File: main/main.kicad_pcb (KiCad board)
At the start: 2 copper layers, 25 x 29 mm, 13 parts, among them J1 PROG, SW1 CONFIG, U1 MSP430FR2311IPW16R, U2 RFM64W

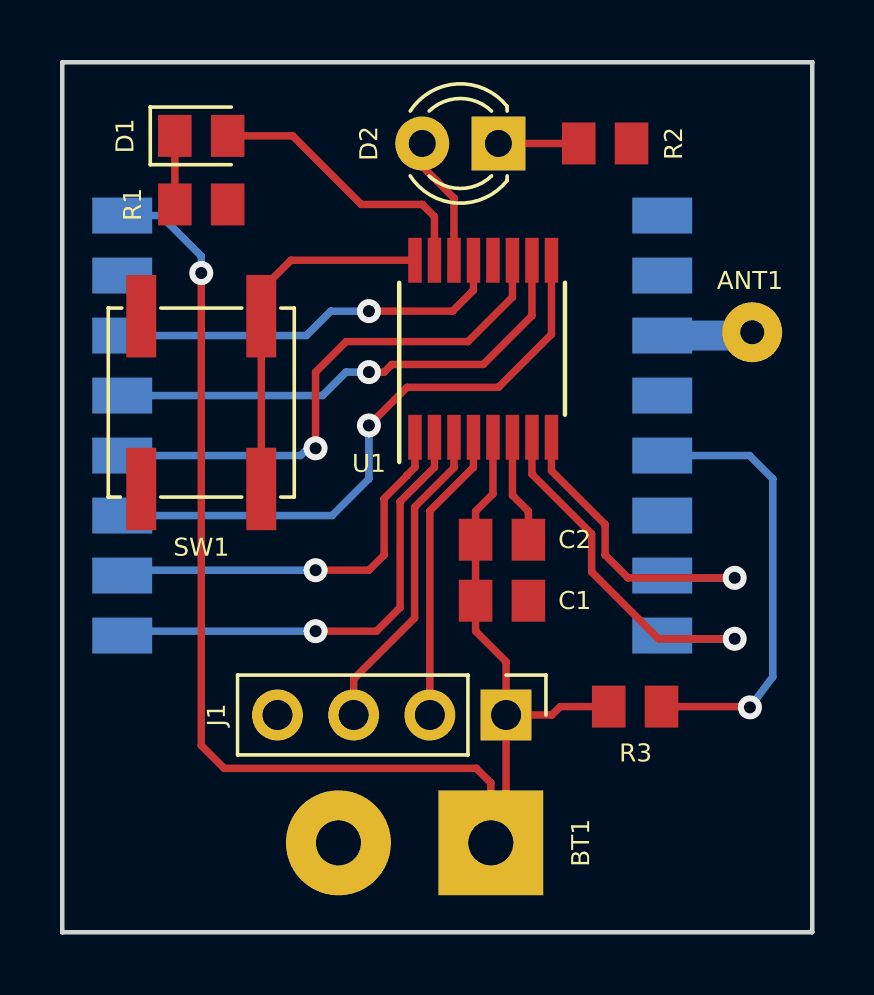
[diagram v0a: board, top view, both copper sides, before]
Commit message: Reduced board size
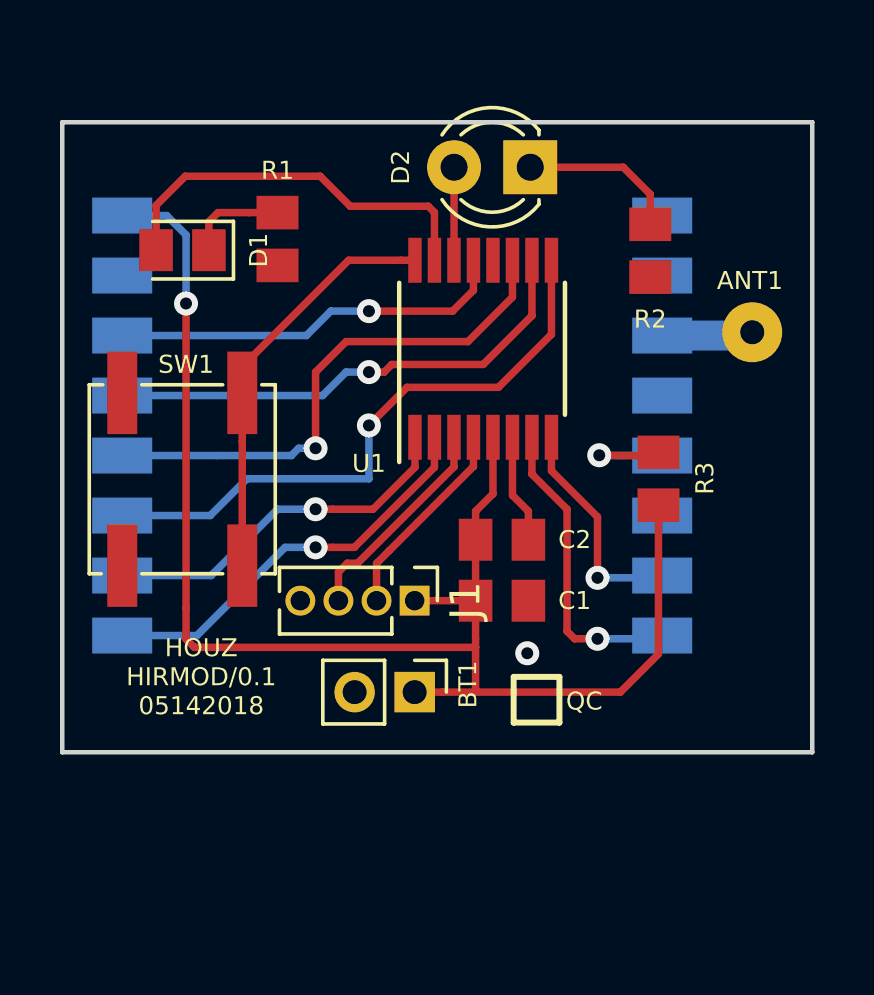
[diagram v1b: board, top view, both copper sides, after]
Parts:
- BT1: footprint Connector_Wire:SolderWirePad_1x02_P5.08mm_Drill1.5mm -> Connector_PinHeader_2.00mm:PinHeader_1x02_P2.00mm_Vertical
- J1: footprint Connector_PinHeader_2.54mm:PinHeader_1x04_P2.54mm_Vertical -> Connector_PinHeader_1.27mm:PinHeader_1x04_P1.27mm_Vertical
- moved R3 7.63 mm to (134.9, 87.9), turned to 90 degrees
- moved BT1 5.63 mm to (126.7, 95.0), turned to 270 degrees
- moved J1 4.88 mm to (126.7, 91.9)
- moved R2 3.88 mm to (134.6, 80.3), turned to 270 degrees
- moved D1 3.86 mm to (119.0, 80.3), turned to 180 degrees
- moved R1 2.79 mm to (122.2, 79.9), turned to 270 degrees
- moved SW1 2.63 mm to (119.0, 87.9)
- moved D2 1.32 mm to (130.6, 77.5)
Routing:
- net /RF_DATA: track 14.8 -> 4.22 mm
- net /IRQ_1: track 11.7 -> 7.66 mm
- net /STATUS: track 9.46 -> 13.3 mm
- net /TST: track 10.6 -> 7.24 mm
- net /RST: track 9.86 -> 6.79 mm
- net /IRQ_0: track 13.5 -> 10.5 mm
- net Net-(D2-Pad1): track 2.68 -> 5.37 mm
- net /POR: track 15.8 -> 13.7 mm
- net /PB_CFG: track 12.2 -> 13.9 mm
- net /IR: track 4.33 -> 3.10 mm
- net /NSS_CFG: track 13.4 -> 12.3 mm
- net Net-(D1-Pad1): track 2.29 -> 3.36 mm
- net GND: vias 0 -> 1
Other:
- board size 25 x 29 mm -> 25 x 21 mm
- board text added: "HOUZ HIRMOD/0.1 05142018"
- board text added: "QC"

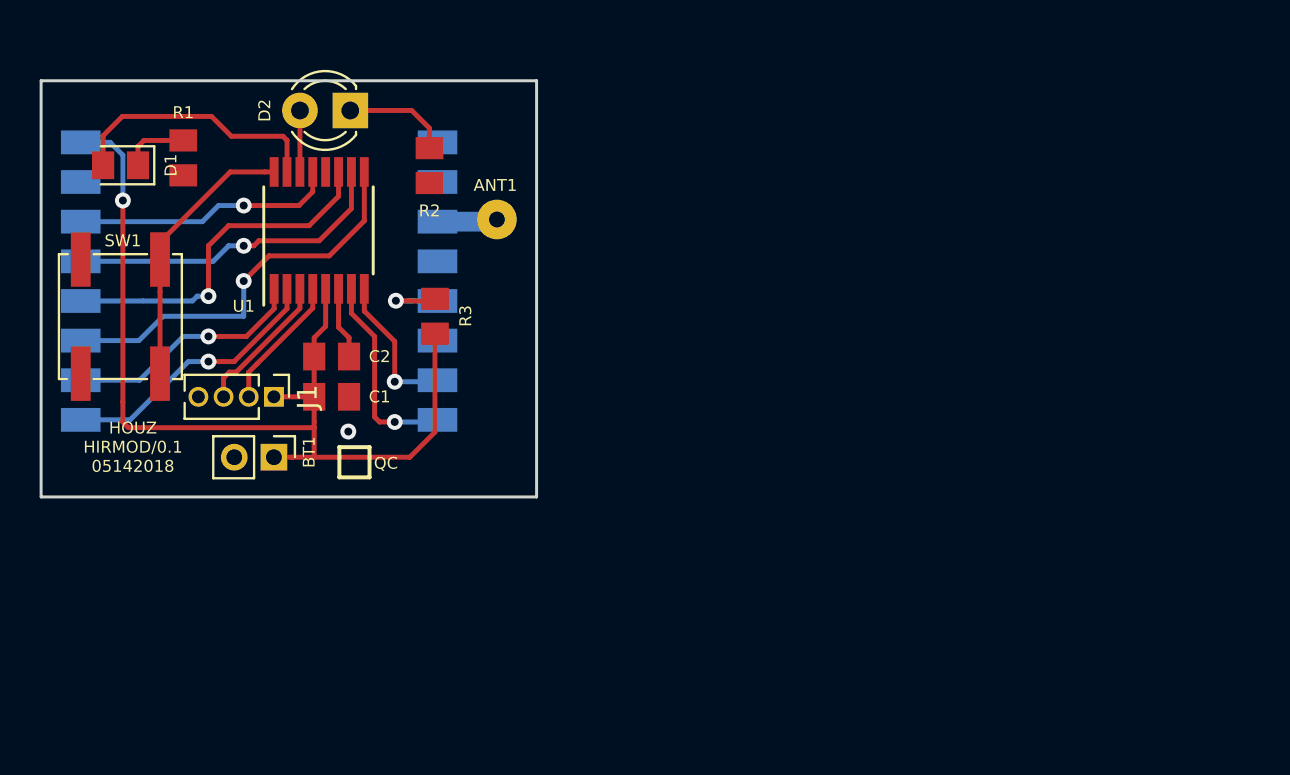
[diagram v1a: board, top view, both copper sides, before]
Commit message: Handmade version of RF BoosterPack for MSP-EXP430FR2311 board
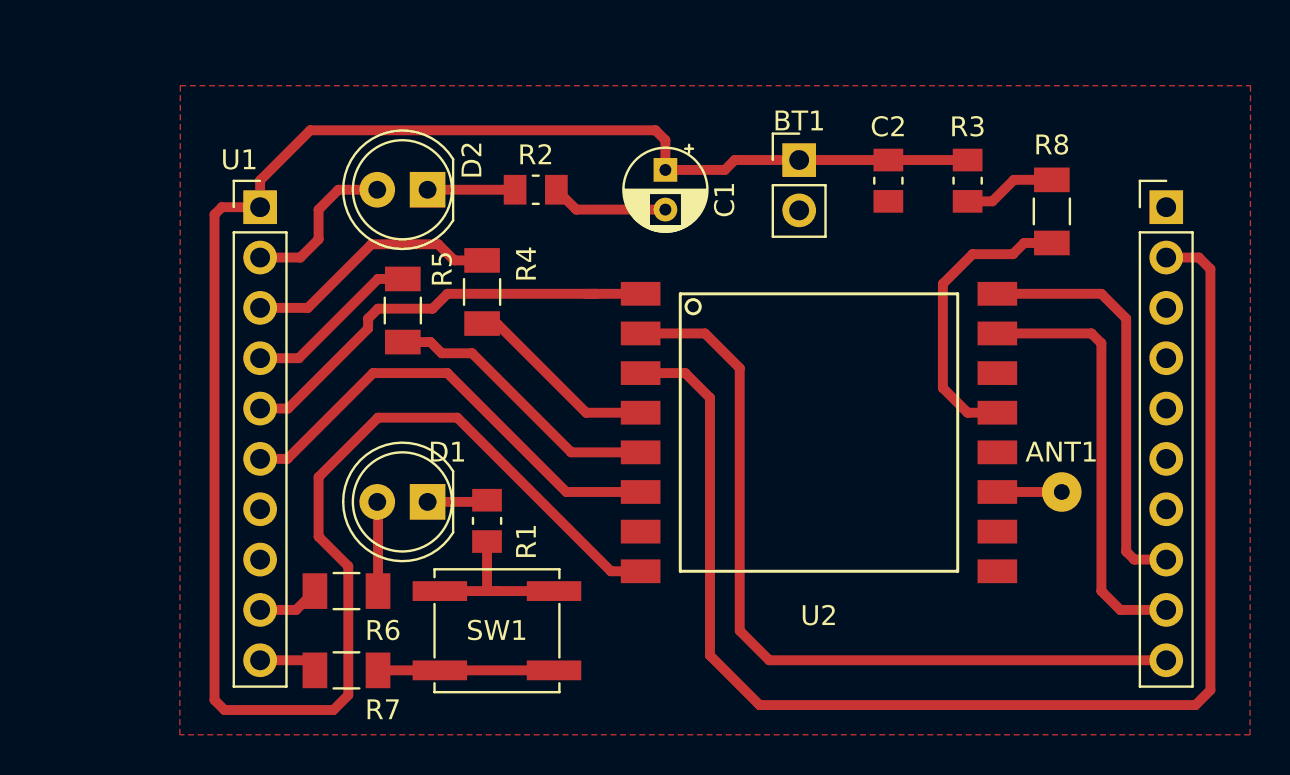
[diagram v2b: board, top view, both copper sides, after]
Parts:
- removed J1: PROG, Connector_PinHeader_1.27mm:PinHeader_1x04_P1.27mm_Vertical
- added R4: 0, Resistor_SMD:R_1206_3216Metric_Pad1.24x1.80mm_HandSolder, F.Cu at (137.2, 86.7)
- added R5: 0, Resistor_SMD:R_1206_3216Metric_Pad1.24x1.80mm_HandSolder, F.Cu at (133.2, 87.6)
- added R6: 0, Resistor_SMD:R_1206_3216Metric_Pad1.24x1.80mm_HandSolder, F.Cu at (130.4, 101.8)
- added R7: 0, Resistor_SMD:R_1206_3216Metric_Pad1.24x1.80mm_HandSolder, F.Cu at (130.4, 105.8)
- added R8: 0, Resistor_SMD:R_1206_3216Metric_Pad1.24x1.80mm_HandSolder, F.Cu at (166.0, 82.6)
- ANT1: footprint Connector_Wire:SolderWirePad_1x01_Drill0.8mm -> Connector_Wire:SolderWirePad_single_0-8mmDrill
- BT1: footprint Connector_PinHeader_2.00mm:PinHeader_1x02_P2.00mm_Vertical -> Connector_PinHeader_2.54mm:PinHeader_1x02_P2.54mm_Vertical
- C1: footprint Capacitor_SMD:C_0805_2012Metric -> Capacitor_THT:CP_Radial_D4.0mm_P2.00mm
- C2: footprint Capacitor_SMD:C_0805_2012Metric -> Capacitor_SMD:C_0805_2012Metric_Pad1.15x1.50mm_HandSolder
- D1: footprint LED_SMD:LED_0805_2012Metric -> LED_THT:LED_D5.0mm
- D2: footprint LED_THT:LED_D3.0mm -> LED_THT:LED_D5.0mm
- R1, R2, R3: footprint Resistor_SMD:R_0805_2012Metric -> Resistor_SMD:R_0805_2012Metric_Pad1.15x1.50mm_HandSolder
- U1: value MSP430FR2311IPW16R -> MSP-EXP430FR2311_BoosterPack; footprint Package_SO:TSSOP-16_4.4x5mm_P0.65mm -> Custom_BoosterPack:BoosterPack_20pins
- U2: moved to F.Cu
- moved ANT1 31.6 mm to (166.5, 96.8)
- moved BT1 30.5 mm to (153.2, 80.0), turned to 0 degrees
- moved C2 29.5 mm to (157.8, 81.0), turned to 270 degrees
- moved U2 29.3 mm to (154.2, 93.8)
- moved R3 27.7 mm to (161.8, 81.0), turned to 270 degrees
- moved SW1 24.7 mm to (138.0, 103.8), turned to 180 degrees
- moved R1 23.9 mm to (137.5, 98.2)
- moved D1 23.0 mm to (134.5, 97.2)
- moved U1 22.4 mm to (148.9, 93.8), turned to 0 degrees
- moved C1 20.4 mm to (146.5, 80.5), turned to 270 degrees
- moved D2 5.59 mm to (134.5, 81.5)
- moved R2 5.49 mm to (140.0, 81.5), turned to 0 degrees
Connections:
- D1 pad 2: /STATUS -> Net-(D1-Pad2)
- R3 pad 2: /RF_DATA -> Net-(R3-Pad2)
- SW1 pad 1: /PB_CFG -> Net-(R7-Pad2)
- U1 pad 1: /NSS_CFG -> VDD
- U1 pad 10: /MOSI -> /PB_CFG
- U1 pad 11: /MISO -> /NSS_CFG
- U1 pad 12: Net-(U1-Pad12) -> /IRQ_1
- U1 pad 13: /SCLK -> /IRQ_0
- U1 pad 14: /IR -> Net-(U1-Pad14)
- U1 pad 15: /STATUS -> Net-(U1-Pad15)
- U1 pad 16: /PB_CFG -> Net-(U1-Pad16)
- U1 pad 2: /POR -> /IR
- U1 pad 3: /TST -> Net-(R4-Pad1)
- U1 pad 4: /RST -> Net-(R5-Pad1)
- U1 pad 5: VDD -> /POR
- U1 pad 6: GND -> /SCLK
- U1 pad 7: /IRQ_0 -> Net-(U1-Pad7)
- U1 pad 8: /IRQ_1 -> Net-(U1-Pad8)
- U1 pad 9: /NSS_DATA -> /STATUS
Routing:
- net VDD: track 50.0 -> 106.6 mm, vias 1 -> 0
- net /NSS_DATA: track 20.3 -> 67.3 mm, vias 1 -> 0
- net /NSS_CFG: track 12.3 -> 41.1 mm, vias 1 -> 0
- net /IRQ_1: track 7.66 -> 21.6 mm, vias 1 -> 0
- net Net-(R4-Pad1): track 0.00 -> 12.9 mm
- net /PB_CFG: track 13.9 -> 2.98 mm
- net /RF_DATA: track 4.22 -> 14.9 mm, vias 1 -> 0
- net GND: track 3.64 -> 14.2 mm, vias 1 -> 0
- net /IRQ_0: track 10.5 -> 21.0 mm, vias 1 -> 0
- net /SCLK: track 13.3 -> 23.5 mm, vias 1 -> 0
- net /STATUS: track 13.3 -> 3.16 mm
- net Net-(R7-Pad2): track 0.00 -> 8.88 mm
- net Net-(R5-Pad1): track 0.00 -> 8.86 mm
- net /POR: track 13.7 -> 22.4 mm, vias 1 -> 0
- net /MISO: track 17.9 -> 9.86 mm, vias 1 -> 0
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- removed copper zone on B.Cu, net GND
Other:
- board outline removed
- net class Default: clearance 0.2 -> 0.25; trace_width 0.25 -> 0.5
- rule trace_clearance: 0.2 -> 0.25
- rule trace_min: 0.1524 -> 0.5
- board text removed: "HOUZ HIRMOD/0.1 05142018"
- board text removed: "QC"

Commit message: Updated BoosterPack board layout
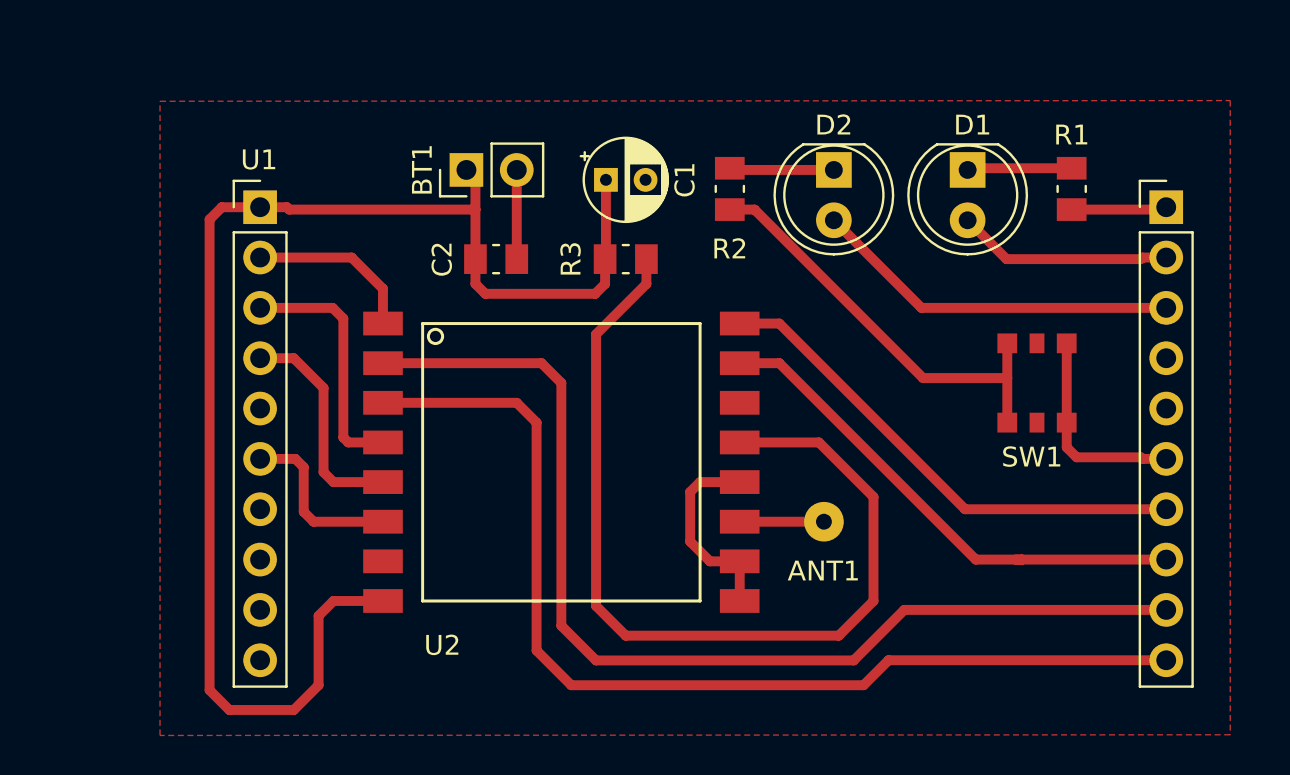
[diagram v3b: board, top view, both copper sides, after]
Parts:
- removed R4, R5, R6, R7, R8: 0, Resistor_SMD:R_1206_3216Metric_Pad1.24x1.80mm_HandSolder
- SW1: footprint Button_Switch_SMD:SW_SPST_EVPBF -> Custom_SwitchButton:SwitchButton_SMD_4x4mm
- moved R1 33.9 mm to (167.0, 81.5)
- moved D1 32.0 mm to (161.8, 80.5), turned to 270 degrees
- moved SW1 30.0 mm to (165.2, 91.2), turned to 270 degrees
- moved D2 20.5 mm to (155.0, 80.5), turned to 270 degrees
- moved C2 20.2 mm to (138.0, 85.0), turned to 0 degrees
- moved R3 17.7 mm to (144.5, 85.0), turned to 0 degrees
- moved BT1 16.8 mm to (136.5, 80.5), turned to 90 degrees
- moved U2 13.1 mm to (141.2, 95.2)
- moved ANT1 12.1 mm to (154.5, 98.2)
- moved R2 9.79 mm to (149.8, 81.5), turned to 270 degrees
- moved C1 3.04 mm to (143.5, 81.0), turned to 0 degrees
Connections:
- D1 pad 2: Net-(D1-Pad2) -> /STATUS
- R3 pad 2: Net-(R3-Pad2) -> /RF_DATA
- SW1 pad 1: Net-(R7-Pad2) -> /PB_CFG
- U1 pad 10: /PB_CFG -> Net-(U1-Pad10)
- U1 pad 11: /NSS_CFG -> /NSS_DATA
- U1 pad 12: /IRQ_1 -> /NSS_CFG
- U1 pad 13: /IRQ_0 -> /IRQ_1
- U1 pad 14: Net-(U1-Pad14) -> /IRQ_0
- U1 pad 15: Net-(U1-Pad15) -> /PB_CFG
- U1 pad 18: Net-(U1-Pad18) -> /IR
- U1 pad 19: /NSS_DATA -> /STATUS
- U1 pad 2: /IR -> /POR
- U1 pad 3: Net-(R4-Pad1) -> /MISO
- U1 pad 4: Net-(R5-Pad1) -> /MOSI
- U1 pad 5: /POR -> Net-(U1-Pad5)
- U1 pad 9: /STATUS -> Net-(U1-Pad9)
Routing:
- net VDD: track 106.6 -> 69.1 mm
- net /RF_DATA: track 14.9 -> 47.0 mm
- net GND: track 14.2 -> 41.0 mm
- net /NSS_DATA: track 67.3 -> 52.7 mm
- net /SCLK: track 23.5 -> 8.83 mm
- net /POR: track 22.4 -> 8.60 mm
- net Net-(R4-Pad1): track 12.9 -> 0.00 mm
- net /NSS_CFG: track 41.1 -> 54.0 mm
- net /IR: track 8.21 -> 18.6 mm
- net Net-(R7-Pad2): track 8.88 -> 0.00 mm
- net Net-(R5-Pad1): track 8.86 -> 0.00 mm
- net /STATUS: track 3.16 -> 10.9 mm
- net /PB_CFG: track 2.98 -> 10.5 mm
- net Net-(R3-Pad2): track 4.70 -> 0.00 mm
- net Net-(D1-Pad2): track 4.52 -> 0.00 mm
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
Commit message: Updated Cap footprint to 5mm
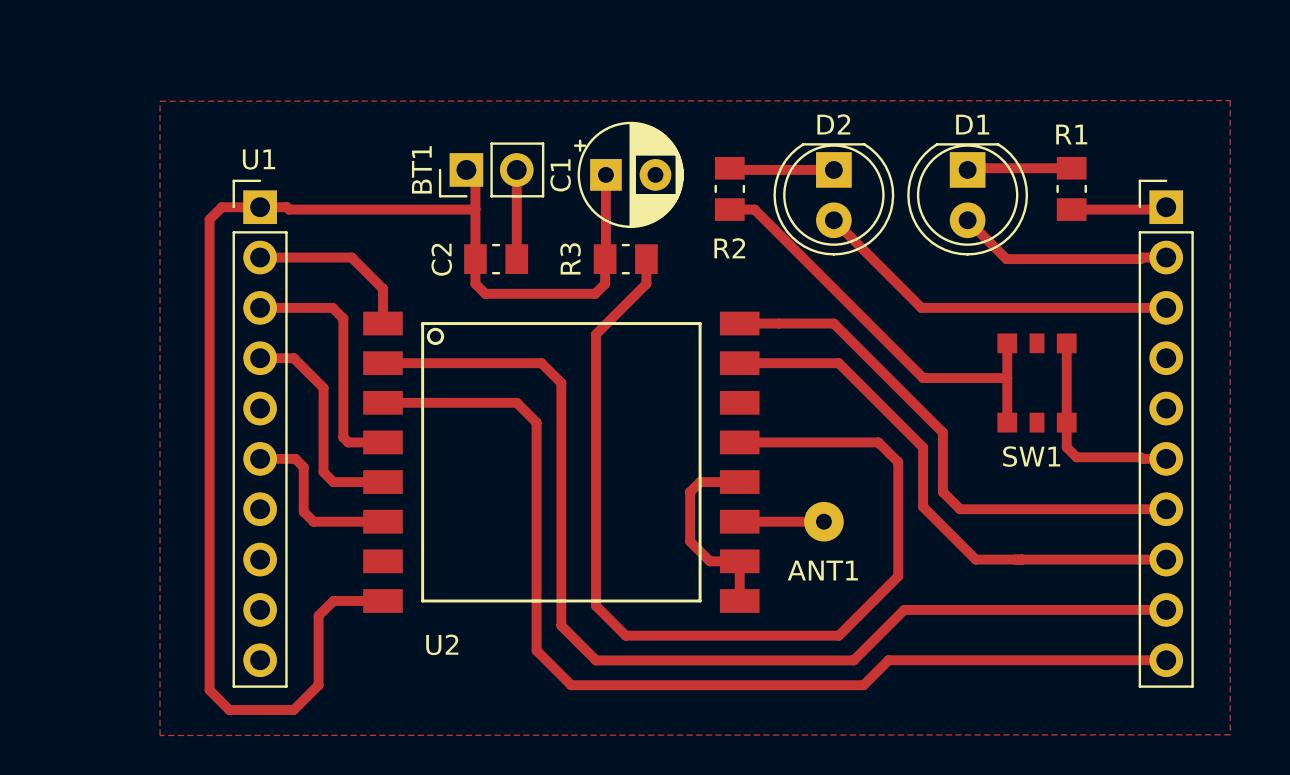
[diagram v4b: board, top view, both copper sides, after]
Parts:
- C1: footprint Capacitor_THT:CP_Radial_D4.0mm_P2.00mm -> Capacitor_THT:CP_Radial_D5.0mm_P2.50mm
- moved C1 0.25 mm to (143.5, 80.8)
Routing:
- net /RF_DATA: track 47.0 -> 49.8 mm
- net /IRQ_1: track 26.0 -> 27.7 mm
- net /IRQ_0: track 25.4 -> 27.2 mm
